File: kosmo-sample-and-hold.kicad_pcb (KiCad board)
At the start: 2 copper layers, 50 x 200 mm, 51 parts, among them Q1 J113, Q2 2N3904, U1 TL074

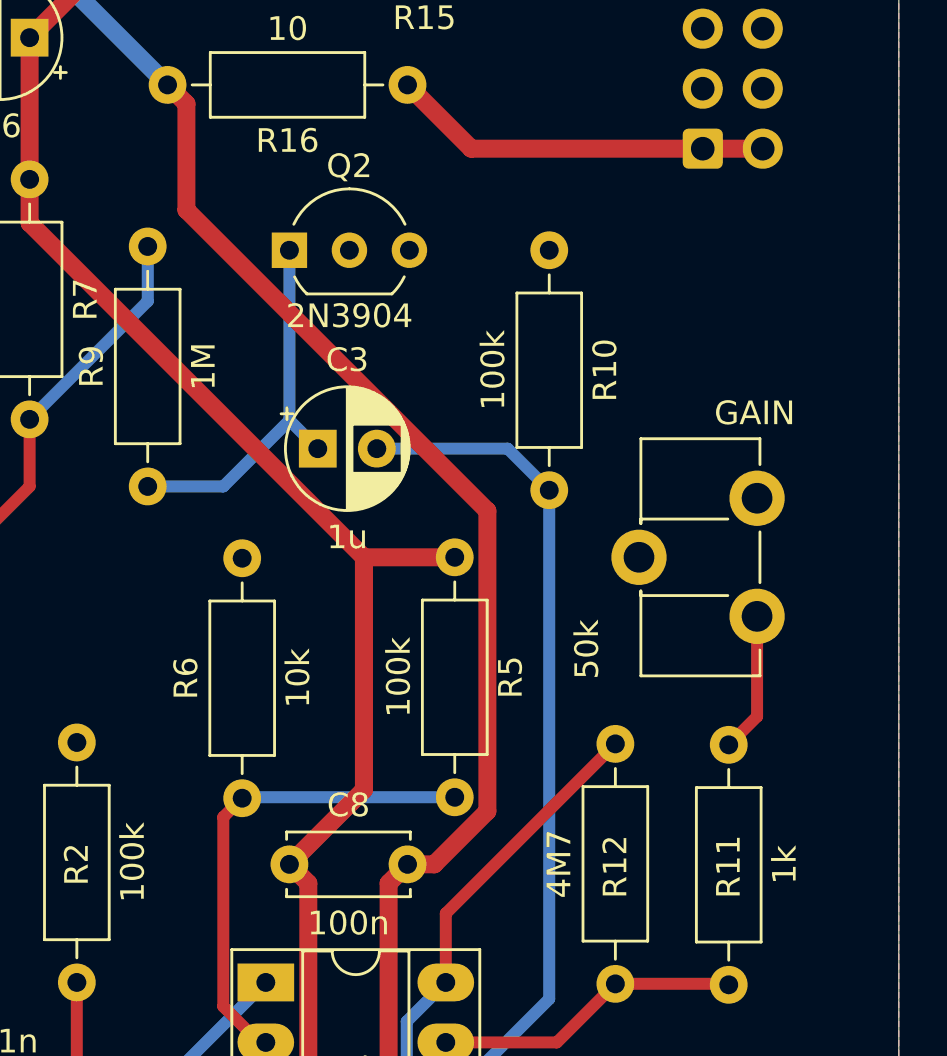
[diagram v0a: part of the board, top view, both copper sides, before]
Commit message: Use BC547 for noise
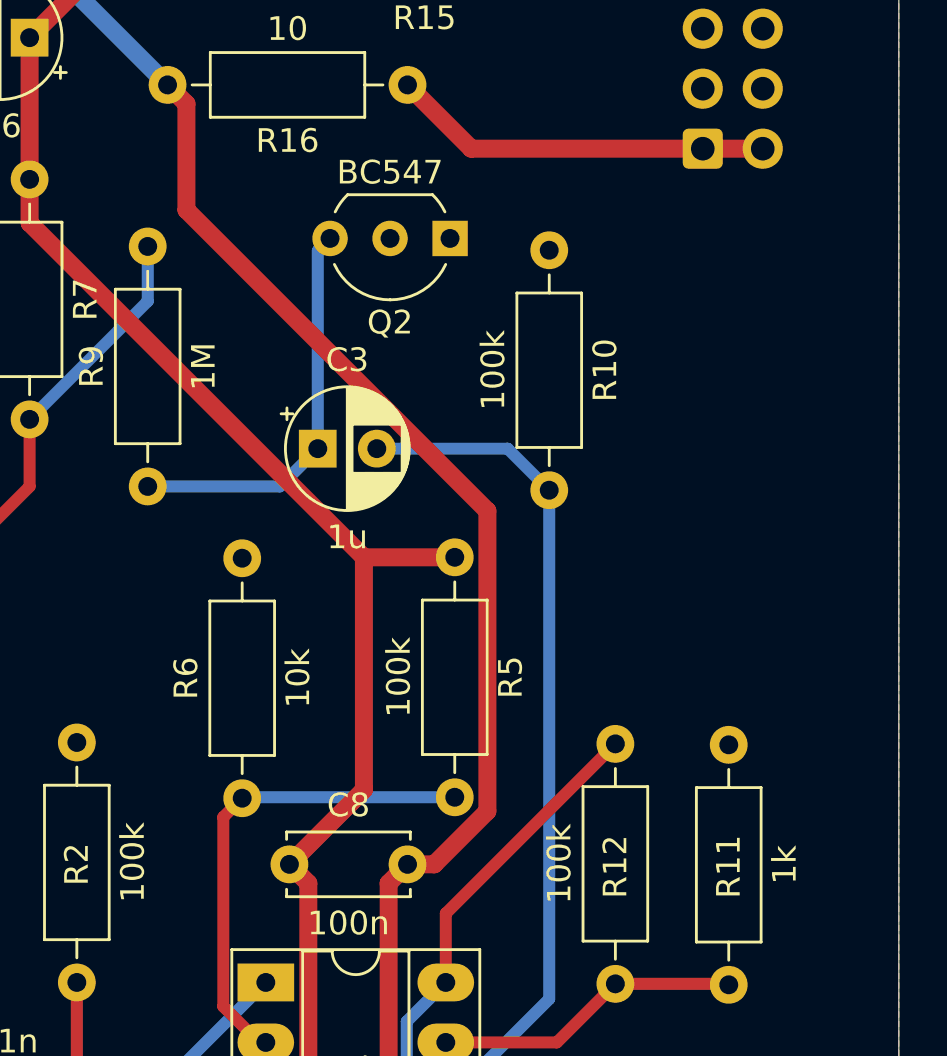
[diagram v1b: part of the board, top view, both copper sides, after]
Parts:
- removed GAIN1: 50k, Potentiometer_THT:Potentiometer_ACP_CA9-H5_Horizontal
- Q2: value 2N3904 -> BC547
- R12: value 4M7 -> 100k
- moved Q2 6.82 mm to (116.0, 81.0), turned to 180 degrees
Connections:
- Q2 pad 1: Net-(C3-Pad1) -> NC
- Q2 pad 3: NC -> Net-(C3-Pad1)
- R11 pad 2: Net-(GAIN1-Pad1) -> GND
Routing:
- net Net-(GAIN1-Pad1): track 5.94 -> 0.00 mm
- net Net-(C3-Pad1): track 16.1 -> 17.0 mm
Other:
- board text added: "Polykit Sample&Hold / Noise v1.0.1 Jan Knipper 2021 github.com/polykit"
- board text removed: "Polykit Sample&Hold / Noise v1.0.0 Jan Knipper 2021 github.com/polykit"
